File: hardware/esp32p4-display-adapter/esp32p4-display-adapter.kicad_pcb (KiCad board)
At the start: 2 copper layers, 20 x 30 mm, 4 parts

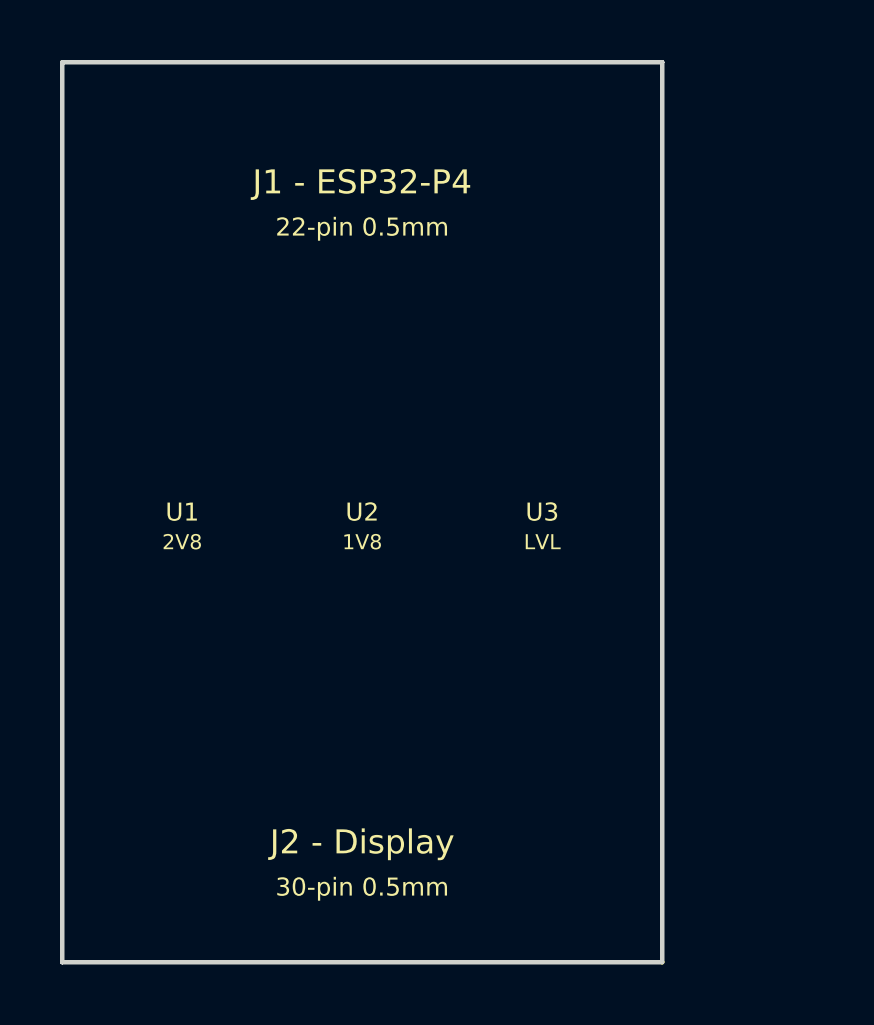
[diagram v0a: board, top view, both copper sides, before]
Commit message: Fix KiCad PCB syntax (remove comments, add UUIDs)
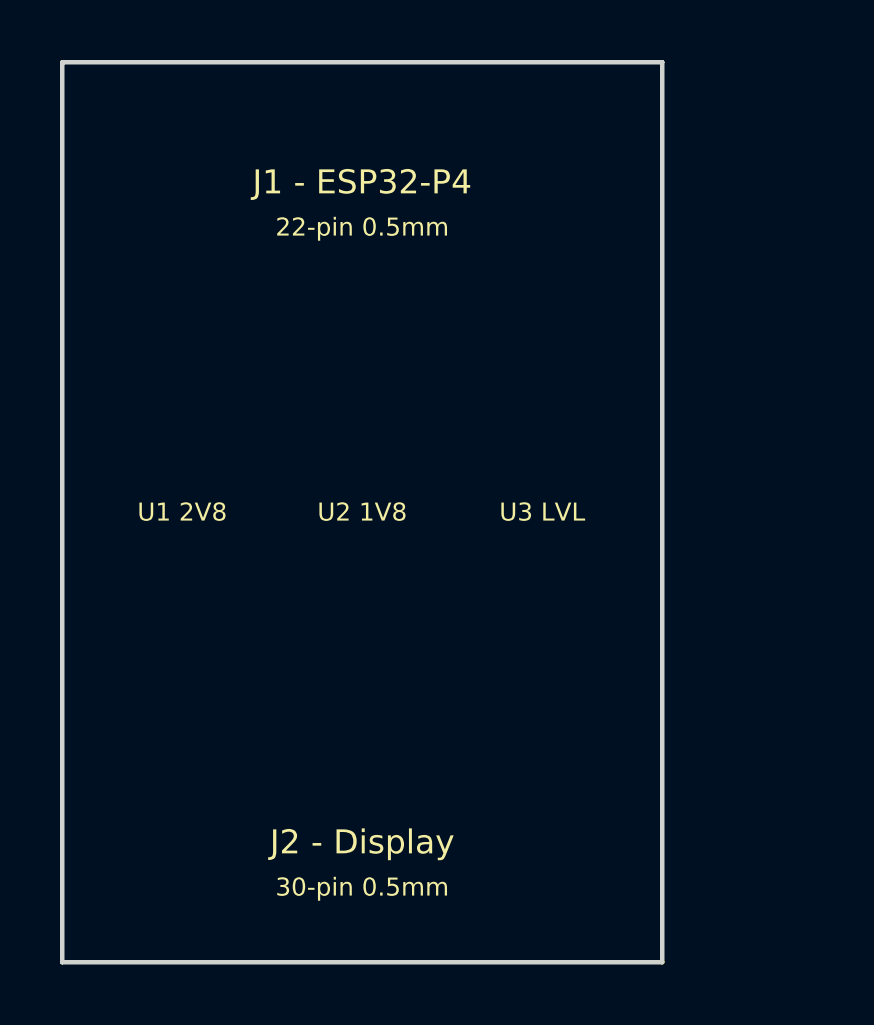
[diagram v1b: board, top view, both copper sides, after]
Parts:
- removed ? (x4): , MountingHole:MountingHole_2.2mm_M2
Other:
- board text added: "MIPI: 100R diff"
- board text added: "U1 2V8"
- board text added: "U2 1V8"
- board text added: "U3 LVL"
- board text removed: "1V8"
- board text removed: "2V8"
- board text removed: "LVL"
- board text removed: "MIPI: 100Ω diff, match ±0.5mm"
- board text removed: "U1"
- board text removed: "U2"
- board text removed: "U3"
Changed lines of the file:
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@@
   (net 18 "LED_A")
   (net 19 "LED_K")
-  ;; Board outline - 20x30mm (compact, both FPC same pitch)
   (gr_rect
     (start 0 0)
@@
     (layer "Edge.Cuts")
   )
-  ;; Mounting holes M2
-  (footprint "MountingHole:MountingHole_2.2mm_M2"
-    (at 2.5 2.5)
-    (layer "F.Cu")
-    (uuid "mh1")
-  )
-  (footprint "MountingHole:MountingHole_2.2mm_M2"
-    (at 17.5 2.5)
-    (layer "F.Cu")
-    (uuid "mh2")
-  )
-  (footprint "MountingHole:MountingHole_2.2mm_M2"
-    (at 2.5 27.5)
-    (layer "F.Cu")
-    (uuid "mh3")
-  )
-  (footprint "MountingHole:MountingHole_2.2mm_M2"
-    (at 17.5 27.5)
-    (layer "F.Cu")
-    (uuid "mh4")
-  )
-  ;; Component placement labels
   (gr_text "J1 - ESP32-P4"
-    (at 10 4)
+    (at 10 4 0)
     (layer "F.SilkS")
     (effects (font (size 0.8 0.8) (thickness 0.12)))
   )
   (gr_text "22-pin 0.5mm"
-    (at 10 5.5)
+    (at 10 5.5 0)
     (layer "F.SilkS")
     (effects (font (size 0.6 0.6) (thickness 0.1)))
   )
   (gr_text "J2 - Display"
-    (at 10 26)
+    (at 10 26 0)
     (layer "F.SilkS")
     (effects (font (size 0.8 0.8) (thickness 0.12)))
   )
   (gr_text "30-pin 0.5mm"
-    (at 10 27.5)
+    (at 10 27.5 0)
     (layer "F.SilkS")
     (effects (font (size 0.6 0.6) (thickness 0.1)))
   )
-  (gr_text "U1"
-    (at 4 15)
+  (gr_text "U1 2V8"
+    (at 4 15 0)
     (layer "F.SilkS")
     (effects (font (size 0.6 0.6) (thickness 0.1)))
   )
-  (gr_text "2V8"
-    (at 4 16)
-    (layer "F.SilkS")
-    (effects (font (size 0.5 0.5) (thickness 0.08)))
-  )
-  (gr_text "U2"
-    (at 10 15)
+  (gr_text "U2 1V8"
+    (at 10 15 0)
     (layer "F.SilkS")
     (effects (font (size 0.6 0.6) (thickness 0.1)))
   )
-  (gr_text "1V8"
-    (at 10 16)
-    (layer "F.SilkS")
-    (effects (font (size 0.5 0.5) (thickness 0.08)))
-  )
-  (gr_text "U3"
-    (at 16 15)
+  (gr_text "U3 LVL"
+    (at 16 15 0)
     (layer "F.SilkS")
     (effects (font (size 0.6 0.6) (thickness 0.1)))
   )
-  (gr_text "LVL"
-    (at 16 16)
-    (layer "F.SilkS")
-    (effects (font (size 0.5 0.5) (thickness 0.08)))
-  )
-  ;; Design rules note
-  (gr_text "MIPI: 100Ω diff, match ±0.5mm"
-    (at 10 21)
+  (gr_text "MIPI: 100R diff"
+    (at 10 21 0)
     (layer "Cmts.User")
     (effects (font (size 0.6 0.6) (thickness 0.1)))

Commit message: Fix ESP32-P4 DSI pinout: 15-pin 1.0mm (same as RPi)
- J1 now 15-pin 1.0mm FPC (was incorrectly 22-pin 0.5mm)
- Added J3 GPIO header for RESET/TP_RESET signals
- Updated pin mapping table to match actual pinout
- Board size 25x30mm
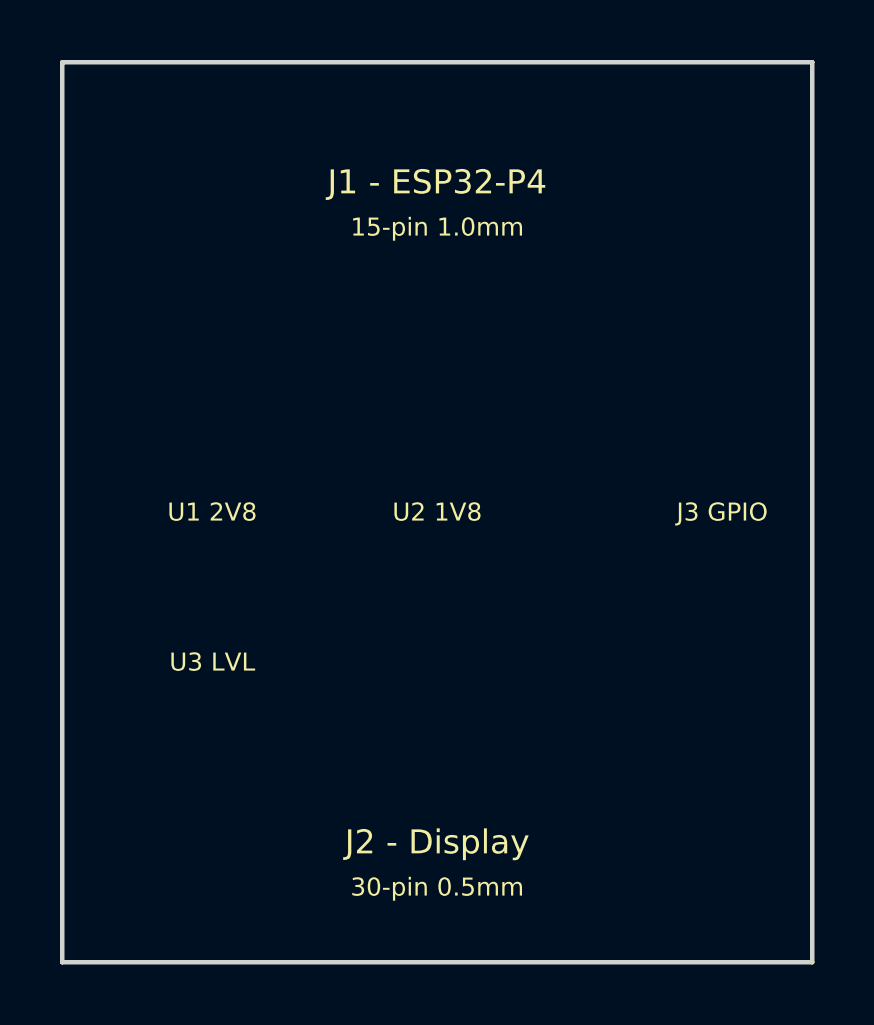
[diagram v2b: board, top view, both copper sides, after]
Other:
- board size 20 x 30 mm -> 25 x 30 mm
- board text added: "15-pin 1.0mm"
- board text added: "J3 GPIO"
- board text removed: "22-pin 0.5mm"
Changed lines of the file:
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@@
     (title "ESP32-P4 DSI to Round Display Adapter")
     (date "2026-04-24")
-    (rev "1.0")
+    (rev "1.1")
     (company "bimmerz.app / OpenCluster")
   )
@@
   (net 0 "")
   (net 1 "GND")
-  (net 2 "ESP_3V3")
+  (net 2 "3V3")
   (net 3 "VCI_2V8")
   (net 4 "IOVCC_1V8")
@@
   (net 15 "TP_RESET_3V3")
   (net 16 "TP_RESET_1V8")
-  (net 17 "TP_INT")
-  (net 18 "LED_A")
-  (net 19 "LED_K")
+  (net 17 "LED_A")
+  (net 18 "LED_K")
   (gr_rect
     (start 0 0)
-    (end 20 30)
+    (end 25 30)
     (stroke (width 0.15) (type solid))
     (fill none)
@@
   )
   (gr_text "J1 - ESP32-P4"
-    (at 10 4 0)
+    (at 12.5 4 0)
     (layer "F.SilkS")
     (effects (font (size 0.8 0.8) (thickness 0.12)))
   )
-  (gr_text "22-pin 0.5mm"
-    (at 10 5.5 0)
+  (gr_text "15-pin 1.0mm"
+    (at 12.5 5.5 0)
     (layer "F.SilkS")
     (effects (font (size 0.6 0.6) (thickness 0.1)))
   )
   (gr_text "J2 - Display"
-    (at 10 26 0)
+    (at 12.5 26 0)
     (layer "F.SilkS")
     (effects (font (size 0.8 0.8) (thickness 0.12)))
   )
   (gr_text "30-pin 0.5mm"
-    (at 10 27.5 0)
+    (at 12.5 27.5 0)
+    (layer "F.SilkS")
+    (effects (font (size 0.6 0.6) (thickness 0.1)))
+  )
+  (gr_text "J3 GPIO"
+    (at 22 15 0)
     (layer "F.SilkS")
     (effects (font (size 0.6 0.6) (thickness 0.1)))
   )
   (gr_text "U1 2V8"
-    (at 4 15 0)
+    (at 5 15 0)
     (layer "F.SilkS")
     (effects (font (size 0.6 0.6) (thickness 0.1)))
   )
   (gr_text "U2 1V8"
-    (at 10 15 0)
+    (at 12.5 15 0)
     (layer "F.SilkS")
     (effects (font (size 0.6 0.6) (thickness 0.1)))
   )
   (gr_text "U3 LVL"
-    (at 16 15 0)
+    (at 5 20 0)
     (layer "F.SilkS")
     (effects (font (size 0.6 0.6) (thickness 0.1)))
   )
   (gr_text "MIPI: 100R diff"
-    (at 10 21 0)
+    (at 12.5 22 0)
     (layer "Cmts.User")
     (effects (font (size 0.6 0.6) (thickness 0.1)))

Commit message: Restore esp32p4-display-adapter (22-pin), add esp32p4-display-adapter-15pin
- esp32p4-display-adapter: 22-pin 0.5mm (your working version restored)
- esp32p4-display-adapter-15pin: NEW - 15-pin 1.0mm (same pinout as RPi)
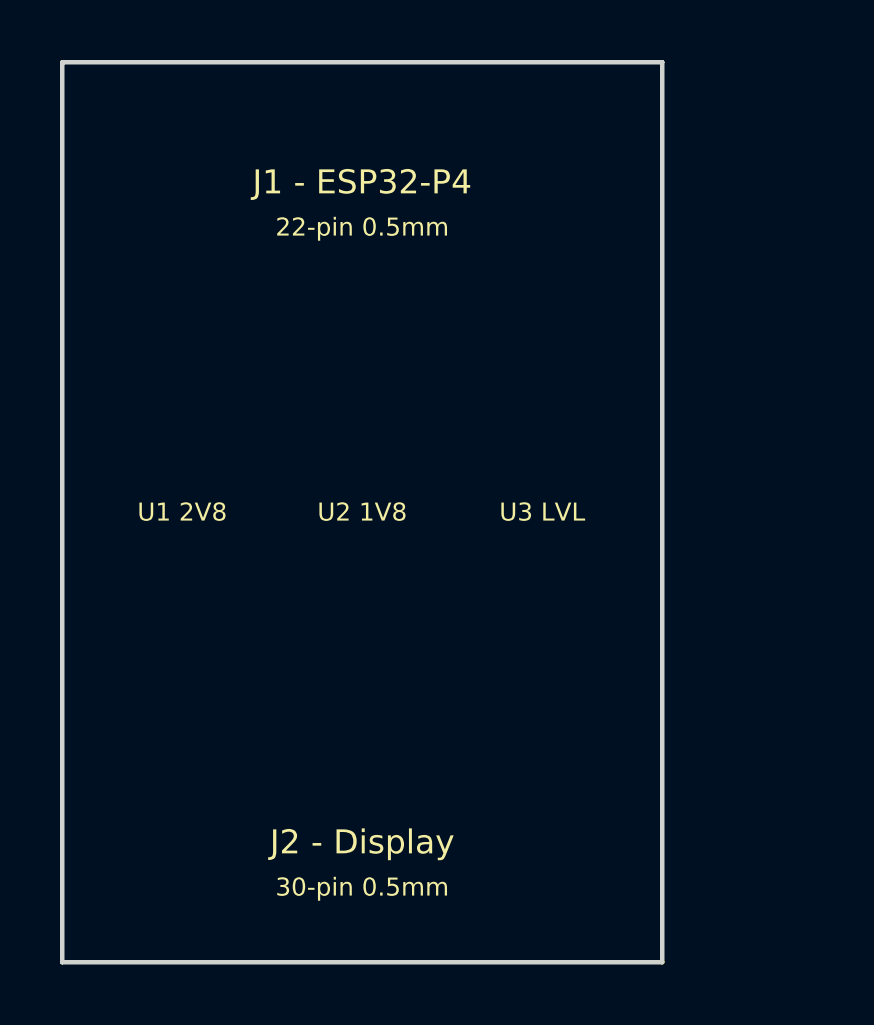
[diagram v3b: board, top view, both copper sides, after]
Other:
- board size 25 x 30 mm -> 20 x 30 mm
- board text added: "22-pin 0.5mm"
- board text removed: "15-pin 1.0mm"
- board text removed: "J3 GPIO"
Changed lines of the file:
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@@
     (title "ESP32-P4 DSI to Round Display Adapter")
     (date "2026-04-24")
-    (rev "1.1")
+    (rev "1.0")
     (company "bimmerz.app / OpenCluster")
   )
@@
   (net 0 "")
   (net 1 "GND")
-  (net 2 "3V3")
+  (net 2 "ESP_3V3")
   (net 3 "VCI_2V8")
   (net 4 "IOVCC_1V8")
@@
   (net 15 "TP_RESET_3V3")
   (net 16 "TP_RESET_1V8")
-  (net 17 "LED_A")
-  (net 18 "LED_K")
+  (net 17 "TP_INT")
+  (net 18 "LED_A")
+  (net 19 "LED_K")
   (gr_rect
     (start 0 0)
-    (end 25 30)
+    (end 20 30)
     (stroke (width 0.15) (type solid))
     (fill none)
@@
   )
   (gr_text "J1 - ESP32-P4"
-    (at 12.5 4 0)
+    (at 10 4 0)
     (layer "F.SilkS")
     (effects (font (size 0.8 0.8) (thickness 0.12)))
   )
-  (gr_text "15-pin 1.0mm"
-    (at 12.5 5.5 0)
+  (gr_text "22-pin 0.5mm"
+    (at 10 5.5 0)
     (layer "F.SilkS")
     (effects (font (size 0.6 0.6) (thickness 0.1)))
   )
   (gr_text "J2 - Display"
-    (at 12.5 26 0)
+    (at 10 26 0)
     (layer "F.SilkS")
     (effects (font (size 0.8 0.8) (thickness 0.12)))
   )
   (gr_text "30-pin 0.5mm"
-    (at 12.5 27.5 0)
-    (layer "F.SilkS")
-    (effects (font (size 0.6 0.6) (thickness 0.1)))
-  )
-  (gr_text "J3 GPIO"
-    (at 22 15 0)
+    (at 10 27.5 0)
     (layer "F.SilkS")
     (effects (font (size 0.6 0.6) (thickness 0.1)))
   )
   (gr_text "U1 2V8"
-    (at 5 15 0)
+    (at 4 15 0)
     (layer "F.SilkS")
     (effects (font (size 0.6 0.6) (thickness 0.1)))
   )
   (gr_text "U2 1V8"
-    (at 12.5 15 0)
+    (at 10 15 0)
     (layer "F.SilkS")
     (effects (font (size 0.6 0.6) (thickness 0.1)))
   )
   (gr_text "U3 LVL"
-    (at 5 20 0)
+    (at 16 15 0)
     (layer "F.SilkS")
     (effects (font (size 0.6 0.6) (thickness 0.1)))
   )
   (gr_text "MIPI: 100R diff"
-    (at 12.5 22 0)
+    (at 10 21 0)
     (layer "Cmts.User")
     (effects (font (size 0.6 0.6) (thickness 0.1)))
